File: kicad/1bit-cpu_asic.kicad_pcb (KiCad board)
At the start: 2 copper layers, 70 x 85 mm, 47 parts, among them J1 USB_C_Receptacle_PowerOnly_6P, J2 Conn_01x11, Q1 2SC1815, Q2 2SC1815, Q3 2SC1815, SW1 SW, SW2 SW, SW3 SW_Push, U1 74HC04, U4 PTC06-1

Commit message: Fix U4's 20&21 pin.
Fix U4's 20&21 pin.
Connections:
- U4 pad 20: +5V -> GND
- U4 pad 21: GND -> +5V
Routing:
- net GND: track 295.3 -> 301.0 mm
- net +5V: track 386.3 -> 391.1 mm

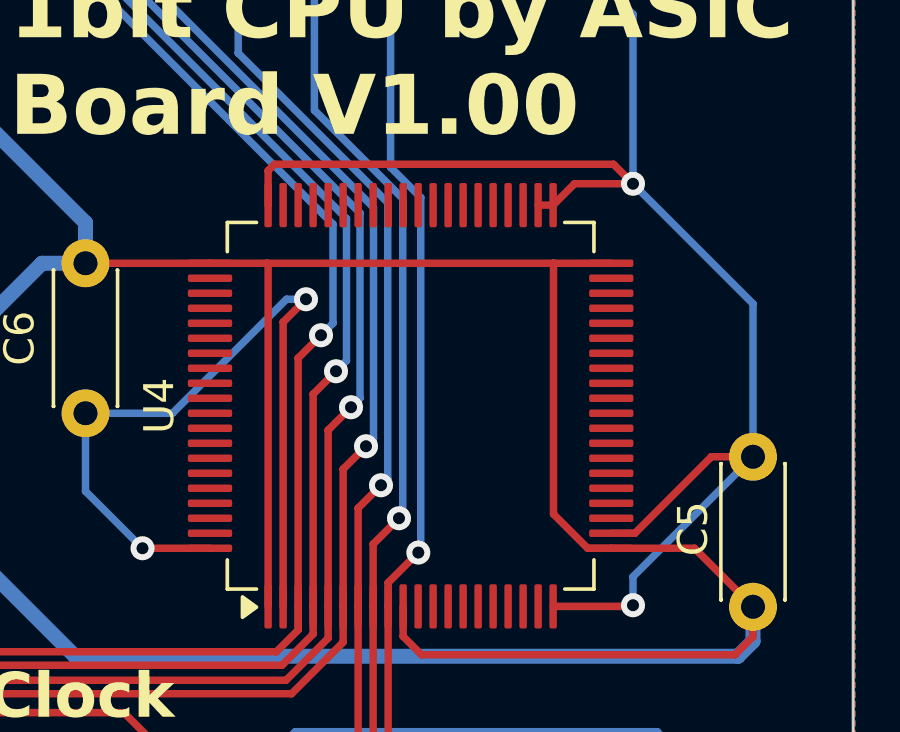
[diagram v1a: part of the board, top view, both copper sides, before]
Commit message: Fix U4's 40&41 pins.
Fix U4's 40&41 pins.
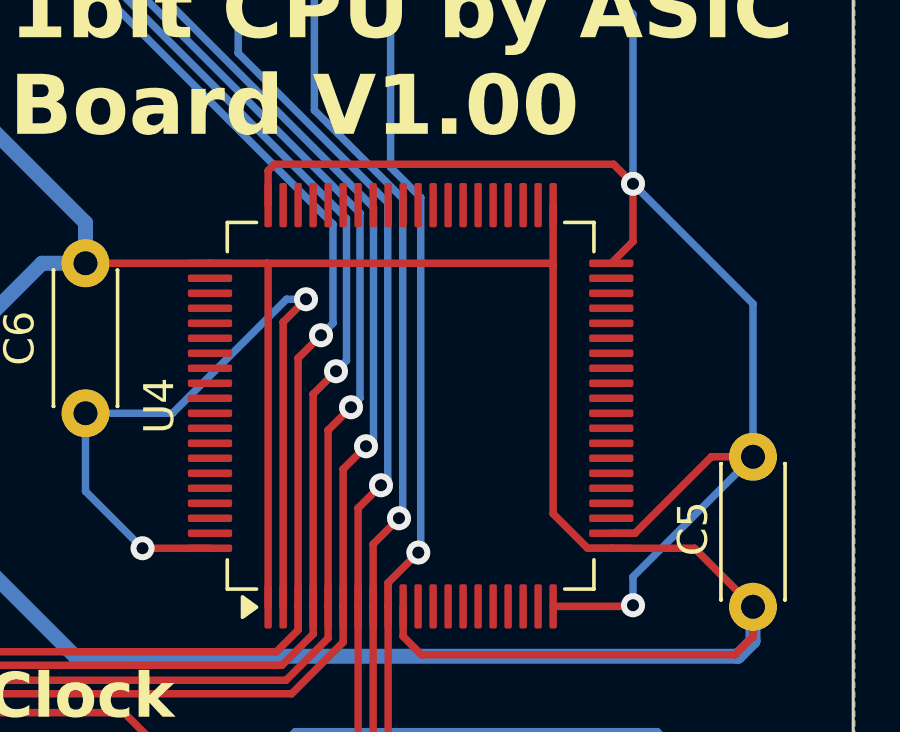
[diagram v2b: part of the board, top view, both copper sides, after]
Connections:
- U4 pad 40: +5V -> GND
- U4 pad 41: GND -> +5V
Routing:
- net GND: track 301.0 -> 300.5 mm
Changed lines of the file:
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@@
 			(layers "F.Cu" "F.Paste" "F.Mask")
 			(roundrect_rratio 0.25)
-			(net 5 "+5V")
+			(net 2 "GND")
 			(pinfunction "VSS")
 			(pintype "power_in")
@@
 			(layers "F.Cu" "F.Paste" "F.Mask")
 			(roundrect_rratio 0.25)
-			(net 2 "GND")
+			(net 5 "+5V")
 			(pinfunction "VDD")
 			(pintype "power_in")
@@
 	)
 	(segment
-		(start 165.4375 77.0625)
-		(end 166.15 76.35)
-		(width 0.25)
-		(layer "F.Cu")
-		(net 2)
-	)
-	(segment
 		(start 129 102.6)
 		(end 129.7 103.3)
@@
 	)
 	(segment
+		(start 167.375 79)
+		(end 168.1 78.275)
+		(width 0.25)
+		(layer "F.Cu")
+		(net 2)
+	)
+	(segment
 		(start 134.1 130.6)
 		(end 134.1 134.7)
@@
 	)
 	(segment
+		(start 168.1 78.275)
+		(end 168.1 76.35)
+		(width 0.25)
+		(layer "F.Cu")
+		(net 2)
+	)
+	(segment
 		(start 125.645 92.38)
 		(end 130.6 92.38)
@@
 	)
 	(segment
-		(start 164.9375 77.0625)
-		(end 165.4375 77.0625)
-		(width 0.25)
-		(layer "F.Cu")
-		(net 2)
-	)
-	(segment
 		(start 130.6 95.7)
 		(end 129 97.3)
@@
 	)
 	(segment
-		(start 166.15 76.35)
-		(end 168.1 76.35)
-		(width 0.25)
-		(layer "F.Cu")
-		(net 2)
-	)
-	(segment
 		(start 168.0625 90.4375)
 		(end 168.1 90.4)
@@
 	)
 	(segment
-		(start 165.45 79)
-		(end 167.375 79)
+		(start 165.4375 79.1)
+		(end 165.4375 77.0625)
 		(width 0.25)
 		(layer "F.Cu")
@@
 	)
 	(segment
+		(start 165.4375 87.34974)
+		(end 165.4375 79.1)
+		(width 0.25)
+		(layer "F.Cu")
+		(net 5)
+	)
+	(segment
 		(start 154 79)
 		(end 149.85 79)
@@
 	(segment
 		(start 166.58776 88.5)
-		(end 165.45 87.36224)
+		(end 165.4375 87.34974)
 		(width 0.25)
 		(layer "F.Cu")
@@
 	)
 	(segment
-		(start 165.45 87.36224)
-		(end 165.45 79)
+		(start 154 79)
+		(end 155.9 79)
 		(width 0.25)
 		(layer "F.Cu")
@@
 	)
 	(segment
-		(start 154 79)
-		(end 155.9 79)
+		(start 131.405 69.905)
+		(end 131.455 69.955)
 		(width 0.25)
 		(layer "F.Cu")
@@
 	)
 	(segment
-		(start 131.405 69.905)
-		(end 131.455 69.955)
+		(start 155.9 79)
+		(end 165.3375 79)
 		(width 0.25)
 		(layer "F.Cu")
@@
 	)
 	(segment
+		(start 165.3375 79)
+		(end 165.4375 79.1)
+		(width 0.25)
+		(layer "F.Cu")
+		(net 5)
+	)
+	(segment
 		(start 167.375 88.5)
 		(end 170.15 88.5)
@@
 	)
 	(segment
-		(start 165.4375 79.0125)
-		(end 165.45 79)
+		(start 167.375 88.5)
+		(end 166.58776 88.5)
 		(width 0.25)
 		(layer "F.Cu")
@@
 	)
 	(segment
-		(start 167.375 88.5)
-		(end 166.58776 88.5)
-		(width 0.25)
-		(layer "F.Cu")
-		(net 5)
-	)
-	(segment
 		(start 155.9375 79.0375)
 		(end 155.9 79)
 		(width 0.25)
 		(layer "F.Cu")
-		(net 5)
-	)
-	(segment
-		(start 155.9 79)
-		(end 165.45 79)
-		(width 0.25)
-		(layer "F.Cu")
